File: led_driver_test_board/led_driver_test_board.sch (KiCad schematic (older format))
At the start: 9 parts

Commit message: Added leds, and three current source types to schematic
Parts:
- removed D? (x8): LED_RGB_SMLP34RGB1W3, symbol LED_RGB_SMLP34RGB1W3
- removed U?: IC_LT3092, symbol IC_LT3092
- added D? (x8): LED_RGB_SMLP34RGB1W3, symbol LED_RGB_SMLP34RGB1W3
- added Q? (x9): Q_NMOS_SSM3K09FULF, symbol Q_NMOS_SSM3K09FULF
- added R? (x27): SMD-RES-0R-1_4W_0603_, symbol SMD-RES-0R-1_4W_0603_
- added U? (x3): CONNEX_CCR_DRIVER_10MA_NSI50010YT1G, symbol CONNEX_CCR_DRIVER_10MA_NSI50010YT1G
- added U? (x3): CONNEX_CCR_DRIVER_20MA_NSI45020T1G, symbol CONNEX_CCR_DRIVER_20MA_NSI45020T1G
- added U? (x3): CONNEX_CCR_DRIVER_30MA_NSI45030AT1G, symbol CONNEX_CCR_DRIVER_30MA_NSI45030AT1G
- added U? (x3): IC_LT3092, symbol IC_LT3092
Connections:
- net labels added: GND, LED1, LED2, LED3, LED4, LED5, LED6, LED7, LED8, LED[1...8], LED_BLUE, LED_DRV_BLUE, LED_DRV_GREEN, LED_DRV_RED, LED_GREEN, LED_RED, PWM1_BLUE, PWM1_GREEN, PWM1_RED, PWM2_BLUE, PWM2_GREEN, PWM2_RED, PWM3_BLUE, PWM3_GREEN, PWM3_RED
- wire segments 6 -> 149

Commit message: Add mcu and routed signals to pins
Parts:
- removed Q? (x6): Q_NMOS_SSM3K09FULF, symbol Q_NMOS_SSM3K09FULF
- removed R? (x15): SMD-RES-0R-1_4W_0603_, symbol SMD-RES-0R-1_4W_0603_
- removed U? (x3): CONNEX_CCR_DRIVER_10MA_NSI50010YT1G, symbol CONNEX_CCR_DRIVER_10MA_NSI50010YT1G
- removed U? (x3): CONNEX_CCR_DRIVER_20MA_NSI45020T1G, symbol CONNEX_CCR_DRIVER_20MA_NSI45020T1G
- removed U? (x3): CONNEX_CCR_DRIVER_30MA_NSI45030AT1G, symbol CONNEX_CCR_DRIVER_30MA_NSI45030AT1G
- removed U? (x3): IC_LT3092, symbol IC_LT3092
- added C? (x9): C_Small, symbol C_Small
- added Q? (x3): Q_NMOS_SSM3K09FULF, symbol Q_NMOS_SSM3K09FULF
- added R? (x12): SMD-RES-0R-1_4W_0603_, symbol SMD-RES-0R-1_4W_0603_
- added U?: connex_EFM32ZG222F16-QFP48, MODULE, symbol connex_EFM32ZG222F16-QFP48
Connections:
- net labels added: +3.3V, BATTERY_ADC, BOOT_RX, BOOT_TX, EXTRA_ADC, FRAME_SYNC, I2C0_SCL, I2C0_SDA, LED_SEL0, LED_SEL1, LED_SEL2, LED_SEL3, LED_SEL4, LED_SEL5, LED_SEL6, LED_SEL7, PWM_BLUE1, PWM_BLUE2, PWM_GREEN1, PWM_GREEN2, PWM_RED1, PWM_RED2, RESET_N, SPI_CLK, SPI_CS, SPI_MOSI, SPI_SIMO
- net labels removed: PWM1_BLUE, PWM1_GREEN, PWM1_RED, PWM2_BLUE, PWM2_GREEN, PWM2_RED, PWM3_BLUE, PWM3_GREEN, PWM3_RED
- wire segments 149 -> 159
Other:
- moved on the sheet: D?, Q?, R?

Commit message: Added bulk caps to zero gecko
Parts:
- removed C? (x9): C_Small, symbol C_Small
- added C1, C2, C4, C5, C6, C9: connex_cap_100NF_0603_10V, symbol connex_cap_100NF_0603_10V
- added C10, C3, C7: connex_cap_10UF_0603_6V3, symbol connex_cap_10UF_0603_6V3
- added C8: connex_cap_1UF_0603_10V, symbol connex_cap_1UF_0603_10V
- U1: renamed from U?; footprint MODULE -> Housings_QFP:TQFP-48_7x7mm_Pitch0.5mm
- gave numbers to parts that had none: 38
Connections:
- wire segments 159 -> 160

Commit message: Initial routing
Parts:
- C1, C10, C2, C3, C4, C5, C6, C7, C8, C9: footprint (none) -> Capacitors_SMD:C_0603
- D1, D2, D3, D4, D5, D6, D7, D8: footprint (none) -> connex_led:led_0404_SMLP34RGB1W3
- Q1, Q2, Q3, Q4, Q5, Q6: footprint (none) -> TO_SOT_Packages_SMD:SC-70
- R1, R10, R11, R12, R13, R14, R15, R16, R17, R18, R19, R2, R20, R21, R22, R23, R24, R3, R4, R5, R6, R7, R8, R9: footprint (none) -> Resistors_SMD:R_0603
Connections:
- net LED_SEL0 is gone; now on net LED8: U1.30 (PC8)
- net LED_SEL1 is gone; now on net LED7: U1.31 (PC9)
- net LED_SEL2 is gone; now on net LED6: U1.32 (PC10)
- net LED_SEL3 is gone; now on net LED5: U1.33 (PC11)
- net LED_SEL4 is gone; now on net LED1: U1.13 (PA8)
- net LED_SEL5 is gone; now on net LED2: U1.14 (PA9)
- net LED_SEL6 is gone; now on net LED3: U1.15 (PA10)
- net LED_SEL7 is gone; now on net LED4: U1.17 (PB11)

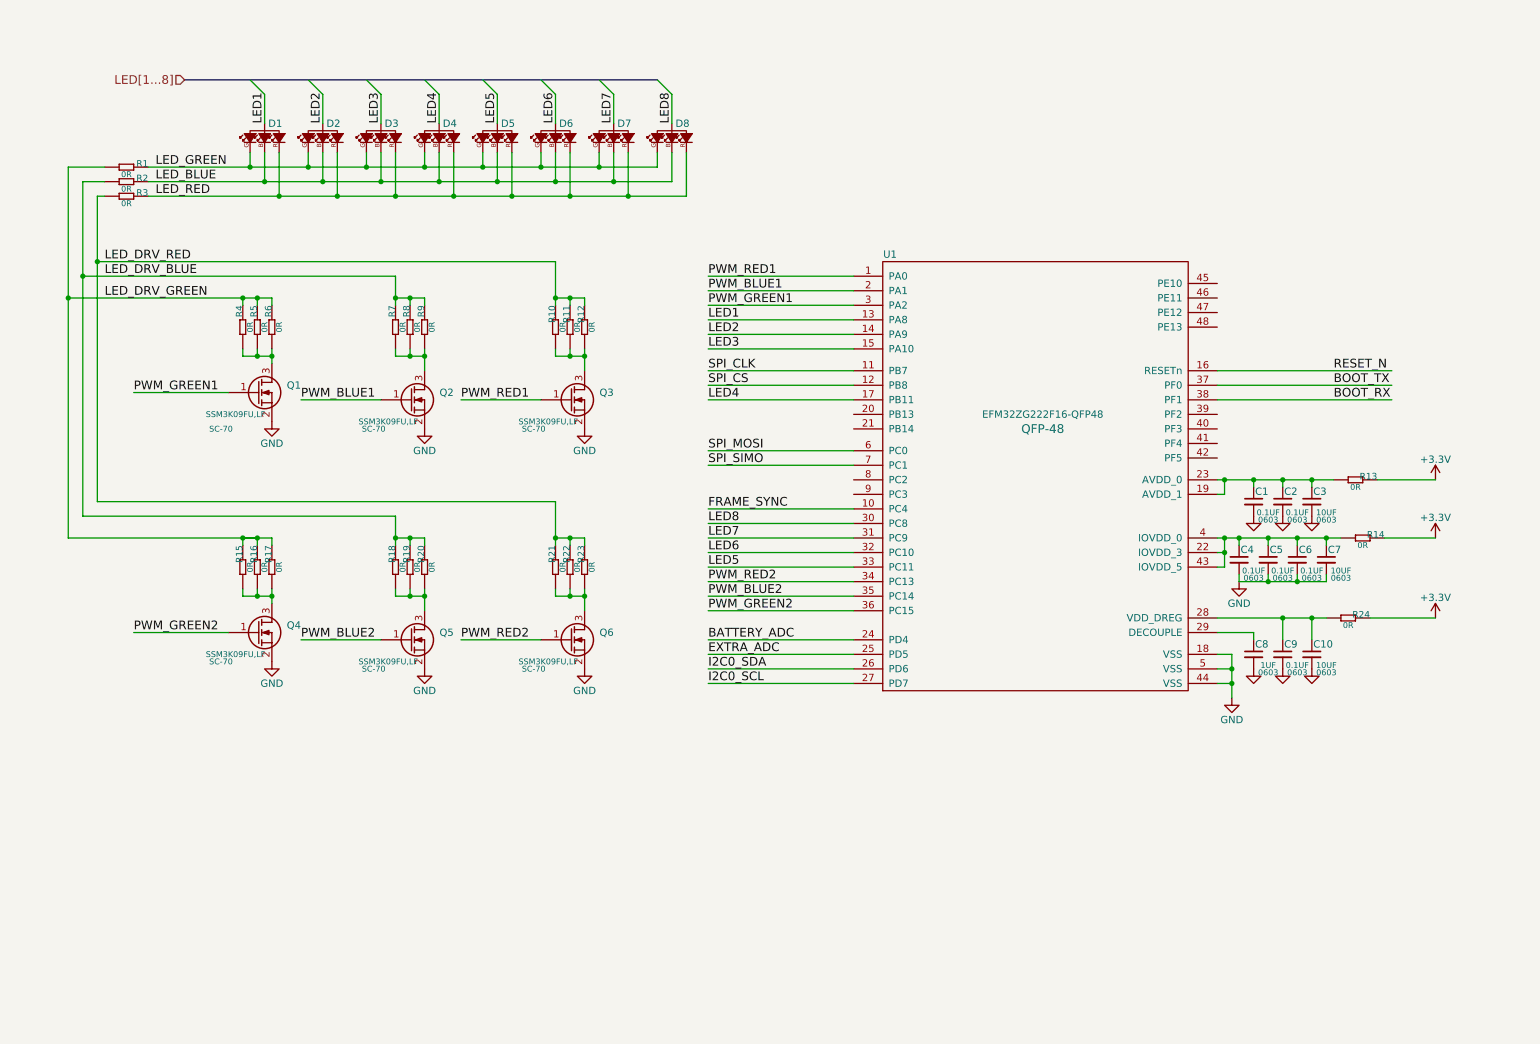
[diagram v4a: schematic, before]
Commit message: Added teset points, caps, headers to the schematic
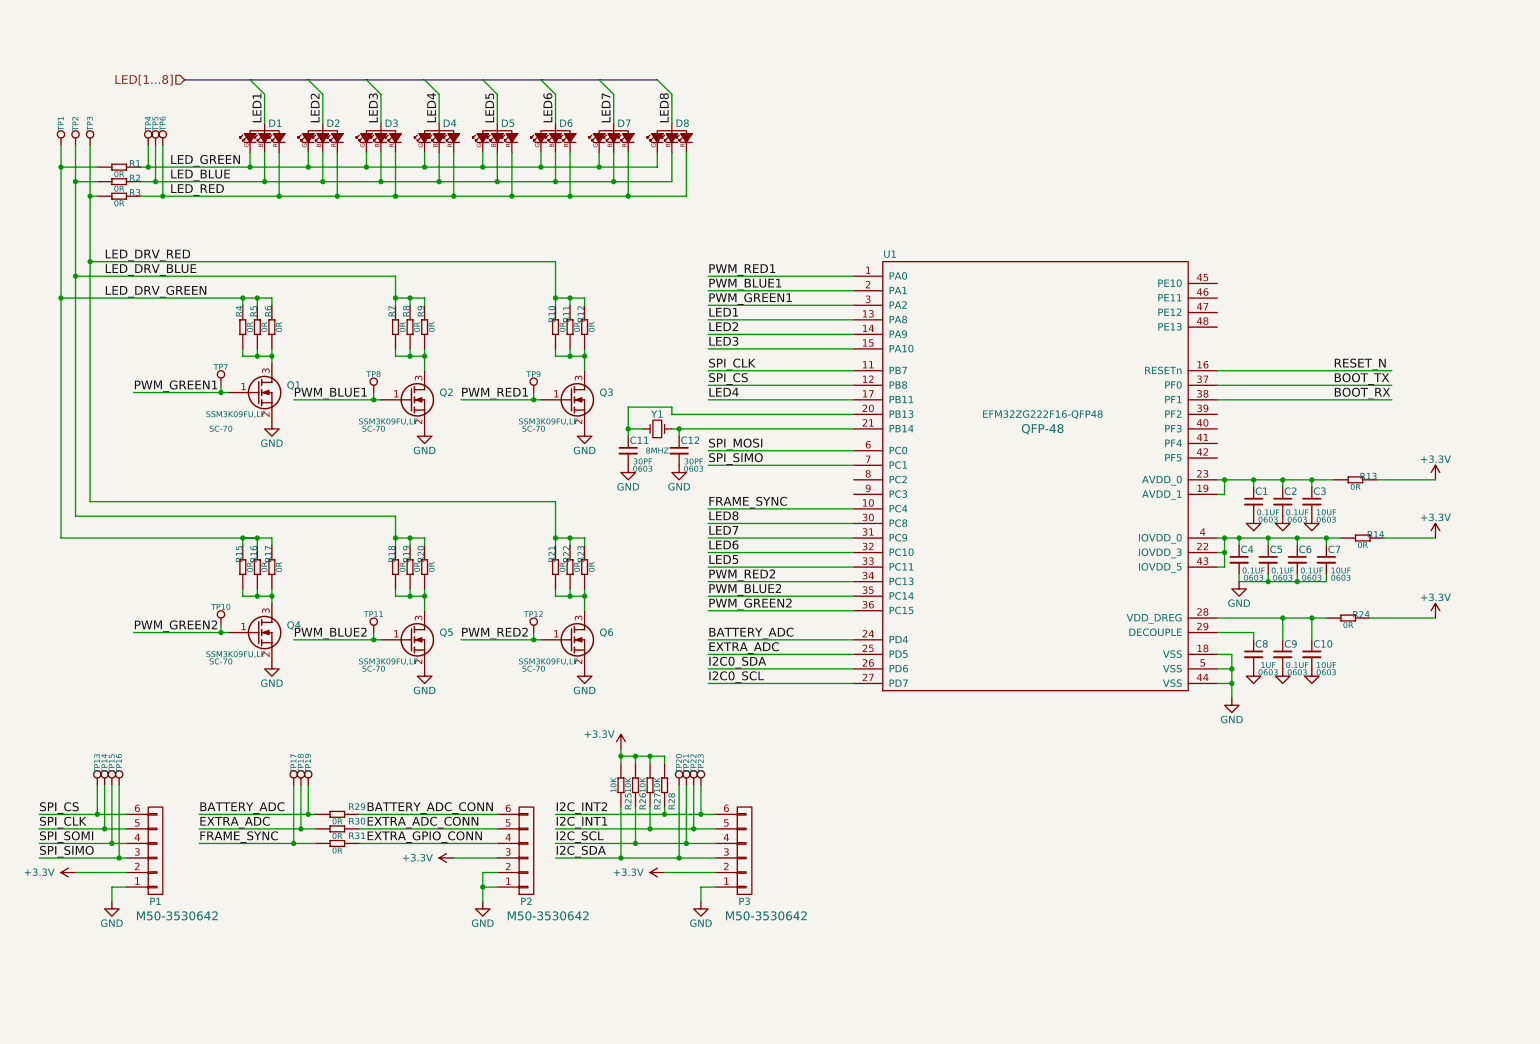
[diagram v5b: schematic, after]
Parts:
- added C11, C12: connex_cap_30PF_0603_50V, symbol connex_cap_30PF_0603_50V
- added P1, P2, P3: CONN_01X06_M50-3530642, symbol CONN_01X06_M50-3530642
- added R25, R26, R27, R28: SMD-RES-10K-1%-1_10W_0603_, symbol SMD-RES-10K-1%-1_10W_0603_
- added R29, R30, R31: SMD-RES-0R-1_4W_0603_, symbol SMD-RES-0R-1_4W_0603_
- added TP1, TP10, TP11, TP12, TP13, TP14, TP15, TP16, TP17, TP18, TP19, TP2, TP20, TP21, TP22, TP23, TP3, TP4, TP5, TP6, TP7, TP8, TP9: test_point_smt, symbol test_point_smt
- added Y1: Crystal_8MHZ_ABM3B-8.000MHZ-B2-T, symbol Crystal_8MHZ_ABM3B-8.000MHZ-B2-T
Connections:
- net +3V3: now also P1.2 (P2), P2.3 (P3), P3.2 (P2), R25.1, R26.1, R27.1, R28.1
- net BATTERY_ADC: now also R29.1, TP19.1
- net EXTRA_ADC: now also R30.1, TP18.1
- net FRAME_SYNC: now also R31.1, TP17.1
- net GND: now also C11.2, C12.2, P1.1 (P1), P2.1 (P1), P2.2 (P2), P3.1 (P1)
- net LED_BLUE: now also TP5.1
- net LED_DRV_BLUE: now also TP2.1
- net LED_DRV_GREEN: now also TP1.1
- net LED_DRV_RED: now also TP3.1
- net LED_GREEN: now also TP4.1
- net LED_RED: now also TP6.1
- net PWM_BLUE1: now also TP8.1
- net PWM_BLUE2: now also TP11.1
- net PWM_GREEN1: now also TP7.1
- net PWM_GREEN2: now also TP10.1
- net PWM_RED1: now also TP9.1
- net PWM_RED2: now also TP12.1
- net SPI_CLK: now also P1.5 (P5), TP14.1
- net SPI_CS: now also P1.6 (P6), TP13.1
- net SPI_SIMO: now also P1.3 (P3), TP16.1
- net at U1.20 (PB13): now also C11.1, Y1.1
- net at U1.21 (PB14): now also C12.1, Y1.3
- new net BATTERY_ADC_CONN: P2.6 (P6), R29.2
- new net EXTRA_ADC_CONN: P2.5 (P5), R30.2
- new net EXTRA_GPIO_CONN: P2.4 (P4), R31.2
- new net I2C_INT1: P3.5 (P5), R27.2, TP22.1
- new net I2C_INT2: P3.6 (P6), R28.2, TP23.1
- new net I2C_SCL: P3.4 (P4), R26.2, TP21.1
- new net I2C_SDA: P3.3 (P3), R25.2, TP20.1
- new net SPI_SOMI: P1.4 (P4), TP15.1
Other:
- moved on the sheet: R1, R2, R3

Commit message: Added crystal and some changes to connector pinout. Continued routing pcb
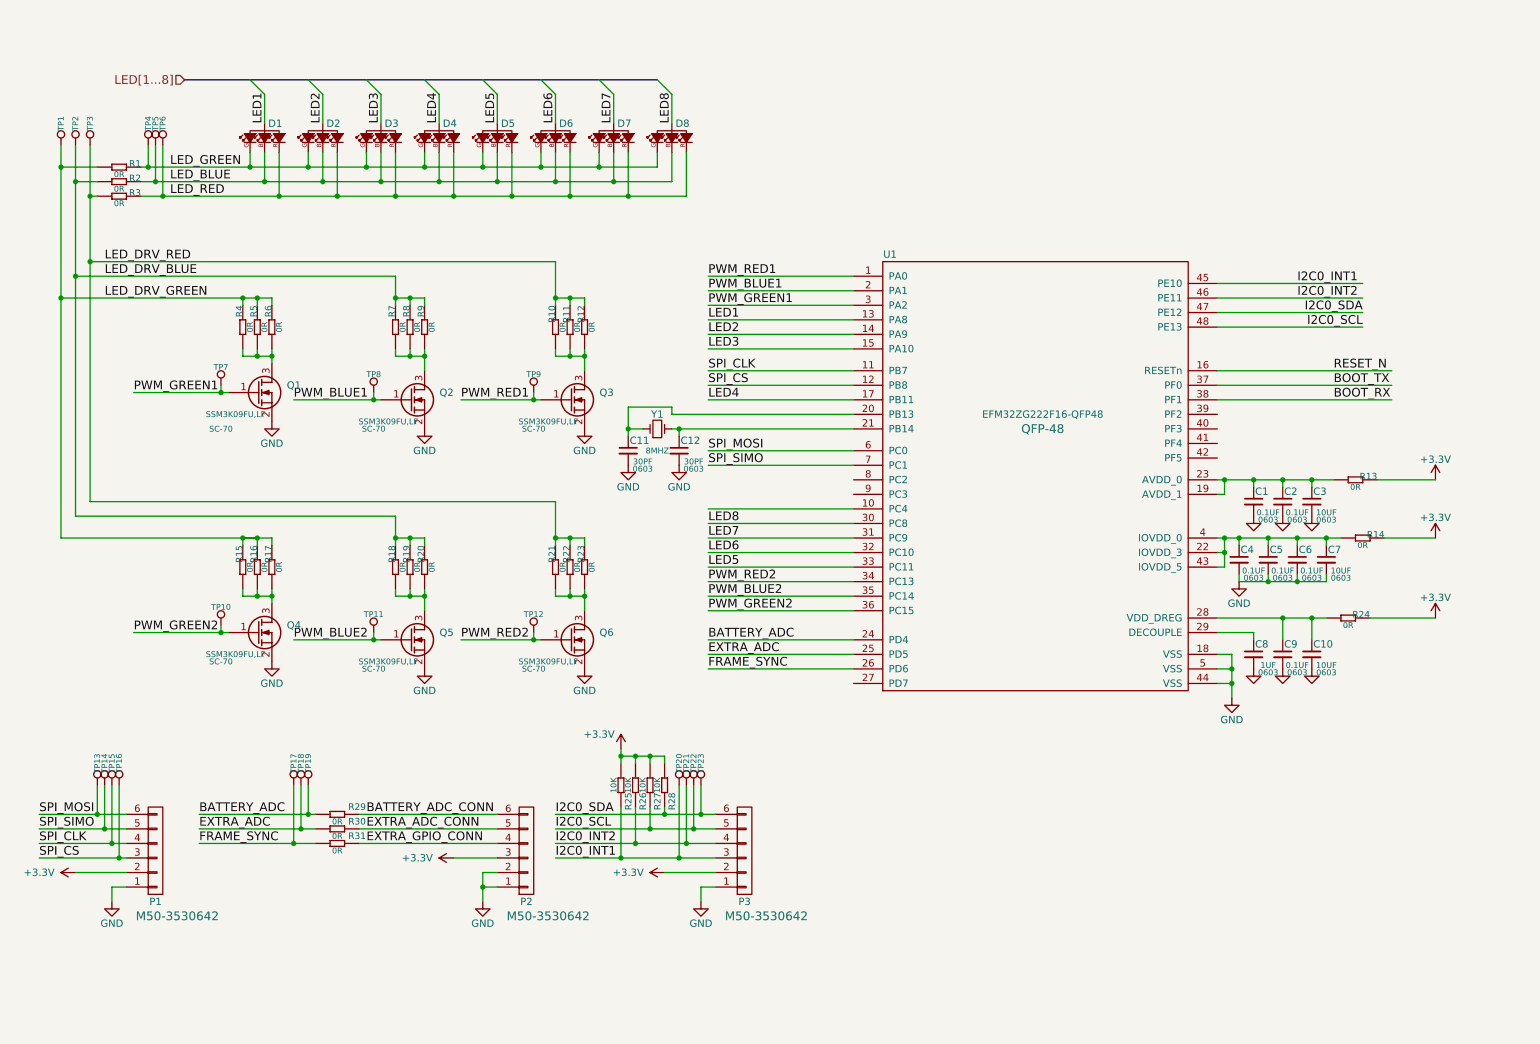
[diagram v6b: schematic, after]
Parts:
- C11, C12: footprint (none) -> Capacitors_SMD:C_0603
- P1, P2, P3: footprint (none) -> Pin_Headers:Pin_Header_Straight_1x06
- R25, R26, R27, R28, R29, R30, R31: footprint (none) -> Resistors_SMD:R_0603
- TP1, TP10, TP11, TP12, TP13, TP14, TP15, TP16, TP17, TP18, TP19, TP2, TP20, TP21, TP22, TP23, TP3, TP4, TP5, TP6, TP7, TP8, TP9: footprint (none) -> connex_test:TEST_POINT_SMD_50MIL
- Y1: footprint (none) -> connex_crystal:CONNEX_CRYSTAL_4SMD_32X50
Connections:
- net I2C_INT1 is gone; now on net I2C0_SCL: P3.5 (P5), R27.2, TP22.1
- net I2C_INT2 is gone; now on net I2C0_SDA: P3.6 (P6), R28.2, TP23.1
- net I2C_SCL is gone; now on net I2C0_INT2: P3.4 (P4), R26.2, TP21.1
- net I2C_SDA is gone; now on net I2C0_INT1: P3.3 (P3), R25.2, TP20.1
- net SPI_SOMI is gone; now on net SPI_CLK: P1.4 (P4), TP15.1
- net FRAME_SYNC: now also U1.26 (PD6); no longer U1.10 (PC4)
- net I2C0_SCL: now also U1.48 (PE13); no longer U1.27 (PD7)
- net I2C0_SDA: now also U1.47 (PE12); no longer U1.26 (PD6)
- net SPI_CLK: no longer P1.5 (P5), TP14.1
- net SPI_CS: now also P1.3 (P3), TP16.1; no longer P1.6 (P6), TP13.1
- net SPI_MOSI: now also P1.6 (P6), TP13.1
- net SPI_SIMO: now also P1.5 (P5), TP14.1; no longer P1.3 (P3), TP16.1
- net I2C0_INT1: now reaches U1.45 (PE10)
- net I2C0_INT2: now reaches U1.46 (PE11)

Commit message: Added regulator to schematic. Routed regulator on board. Adjusted headers
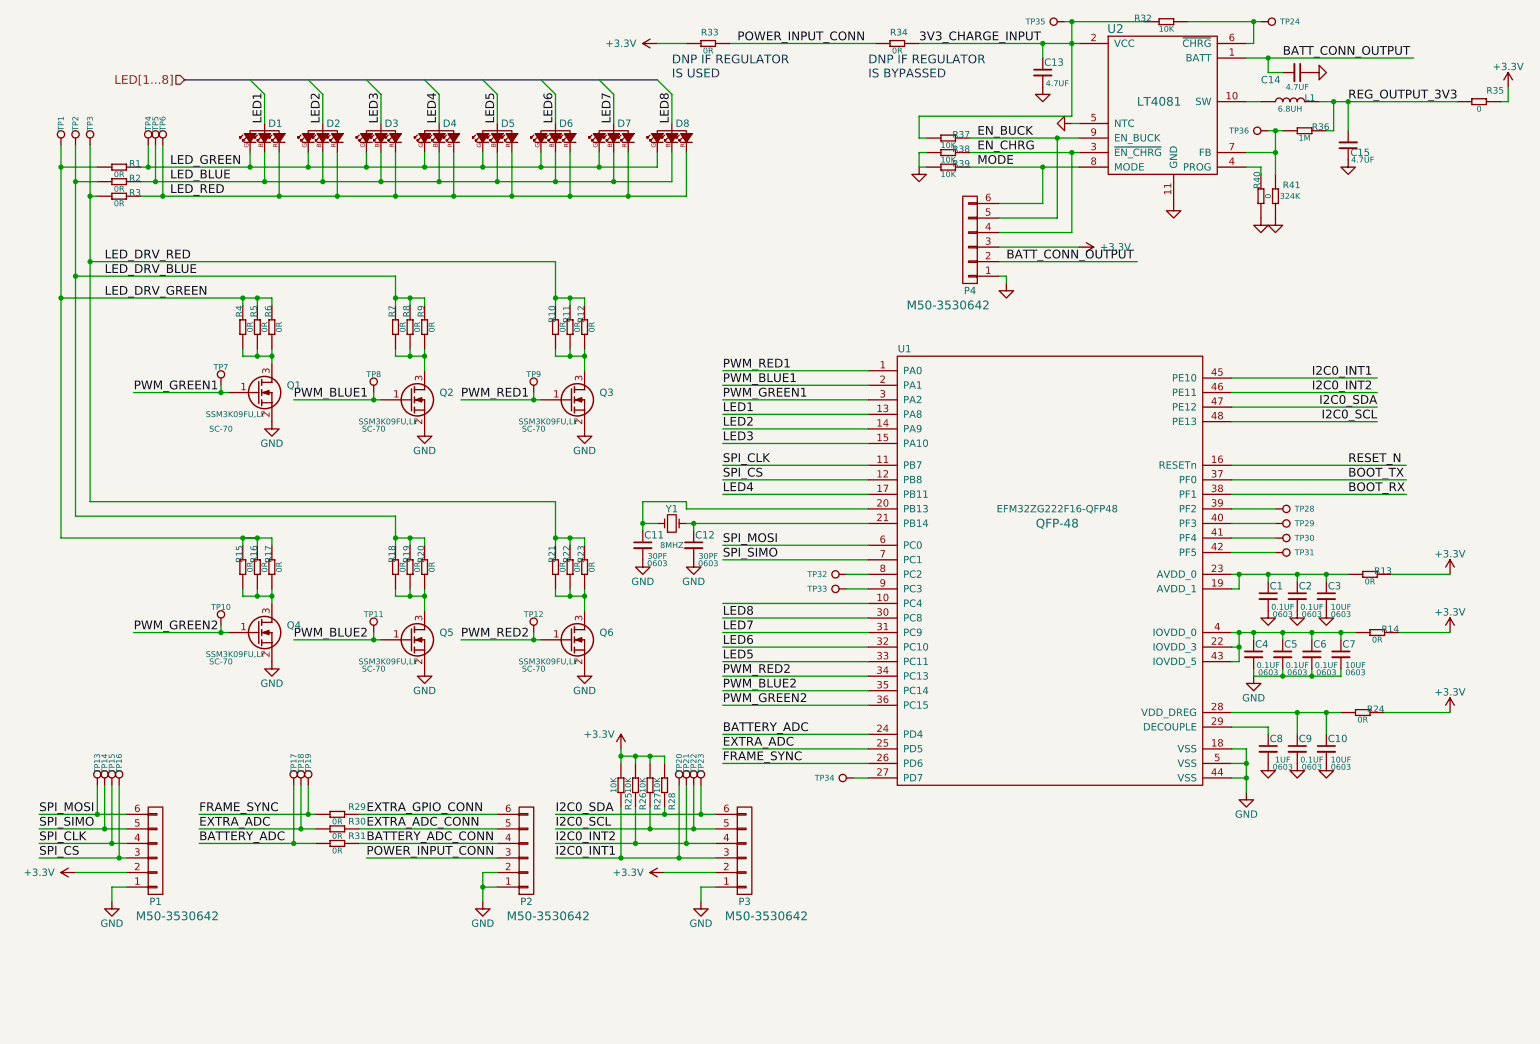
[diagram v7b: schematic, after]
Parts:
- added C13, C14, C15: CONNEX-SMD-CAP-4700NF-0603, Capacitors_SMD:C_0603, symbol CONNEX-SMD-CAP-4700NF-0603
- added L1: CONNEX-SMD-INDUCTOR-6R8M-0603, connex_inductor:L_0603, symbol CONNEX-SMD-INDUCTOR-6R8M-0603
- added P4: CONN_01X06_M50-3530642, Pin_Headers:Pin_Header_Straight_1x06, symbol CONN_01X06_M50-3530642
- added R32, R37, R38, R39: SMD-RES-10K-1%-1_10W_0603_, Resistors_SMD:R_0603, symbol SMD-RES-10K-1%-1_10W_0603_
- added R33, R34: SMD-RES-0R-1_4W_0603_, Resistors_SMD:R_0603, symbol SMD-RES-0R-1_4W_0603_
- added R35, R40: CONNEX-SMD-RES-0-0603, Resistors_SMD:R_0603, symbol CONNEX-SMD-RES-0-0603
- added R36: CONNEX-SMD-RES-1M-0603, Resistors_SMD:R_0603, symbol CONNEX-SMD-RES-1M-0603
- added R41: CONNEX-SMD-RES-324K-0603, Resistors_SMD:R_0603, symbol CONNEX-SMD-RES-324K-0603
- added TP24, TP28, TP29, TP30, TP31, TP32, TP33, TP34, TP35, TP36: test_point_smt, connex_test:TEST_POINT_SMD_50MIL, symbol test_point_smt
- added U2: CONNEX_REGUL_LT4081, connex_smd_misc:CONNEX_DFN_10PIN_3MMX3MM, symbol CONNEX_REGUL_LT4081
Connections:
- net +3V3: now also P4.3 (P3), R33.1, R35.2; no longer P2.3 (P3)
- net BATTERY_ADC: now also R31.1, TP17.1; no longer R29.1, TP19.1
- net BATTERY_ADC_CONN: now also P2.4 (P4), R31.2; no longer P2.6 (P6), R29.2
- net EXTRA_GPIO_CONN: now also P2.6 (P6), R29.2; no longer P2.4 (P4), R31.2
- net FRAME_SYNC: now also R29.1, TP19.1; no longer R31.1, TP17.1
- net GND: now also C13.2, C14.1, C15.1, P4.1 (P1), R38.2, R39.2, R40.1, R41.2, U2.11 (GND), U2.5 (NTC)
- net at U1.27 (PD7): now also TP34.1
- net at U1.39 (PF2): now also TP28.1
- net at U1.40 (PF3): now also TP29.1
- net at U1.41 (PF4): now also TP30.1
- net at U1.42 (PF5): now also TP31.1
- net at U1.8 (PC2): now also TP32.1
- net at U1.9 (PC3): now also TP33.1
- new net: L1.1, U2.10 (SW)
- new net: R40.2, U2.4 (PROG)
- new net: R32.1, TP24.1, U2.6 (~CHRG~)
- new net: R36.1, R41.1, TP36.1, U2.7 (FB)
- new net 3V3_CHARGE_INPUT: C13.1, R32.2, R34.2, R37.2, TP35.1, U2.2 (VCC)
- new net BATT_CONN_OUTPUT: C14.2, P4.2 (P2), U2.1 (BATT)
- new net EN_BUCK: P4.5 (P5), R37.1, U2.9 (EN_BUCK)
- new net EN_CHRG: P4.4 (P4), R38.1, U2.3 (~EN_CHRG~)
- new net MODE: P4.6 (P6), R39.1, U2.8 (MODE)
- new net POWER_INPUT_CONN: P2.3 (P3), R33.2, R34.1
- new net REG_OUTPUT_3V3: C15.2, L1.2, R35.1, R36.2
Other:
- note added: "DNP IF REGULATOR \nIS BYPASSED"
- note added: "DNP IF REGULATOR \nIS USED"
- moved on the sheet: C1, C10, C11, C12, C2, C3, C4, C5, C6, C7, C8, C9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
